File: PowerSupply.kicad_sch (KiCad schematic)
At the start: 45 parts, among them U1 LM399, U2 LT1001

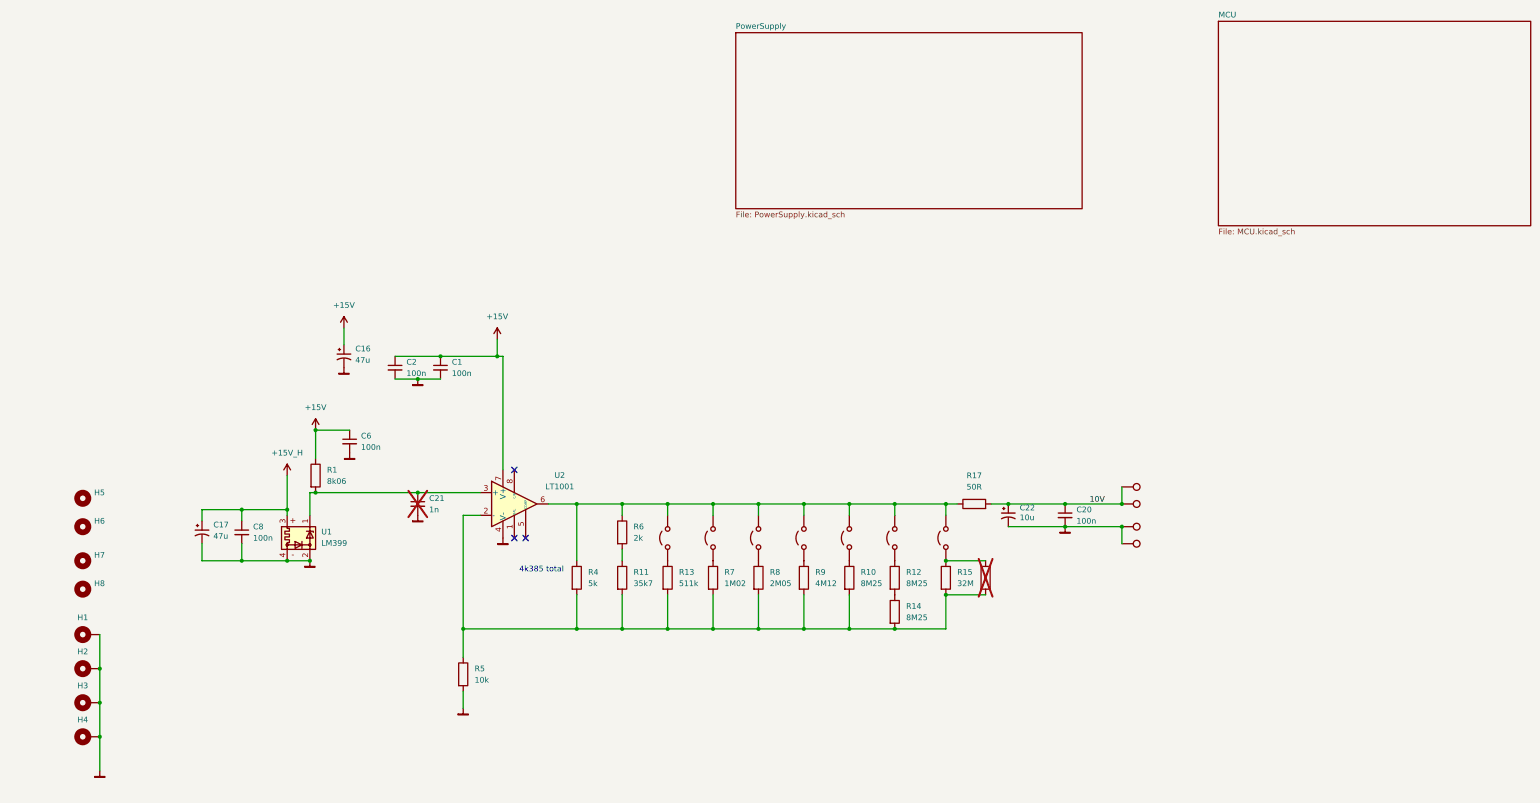
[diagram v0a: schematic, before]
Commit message: Added MCU
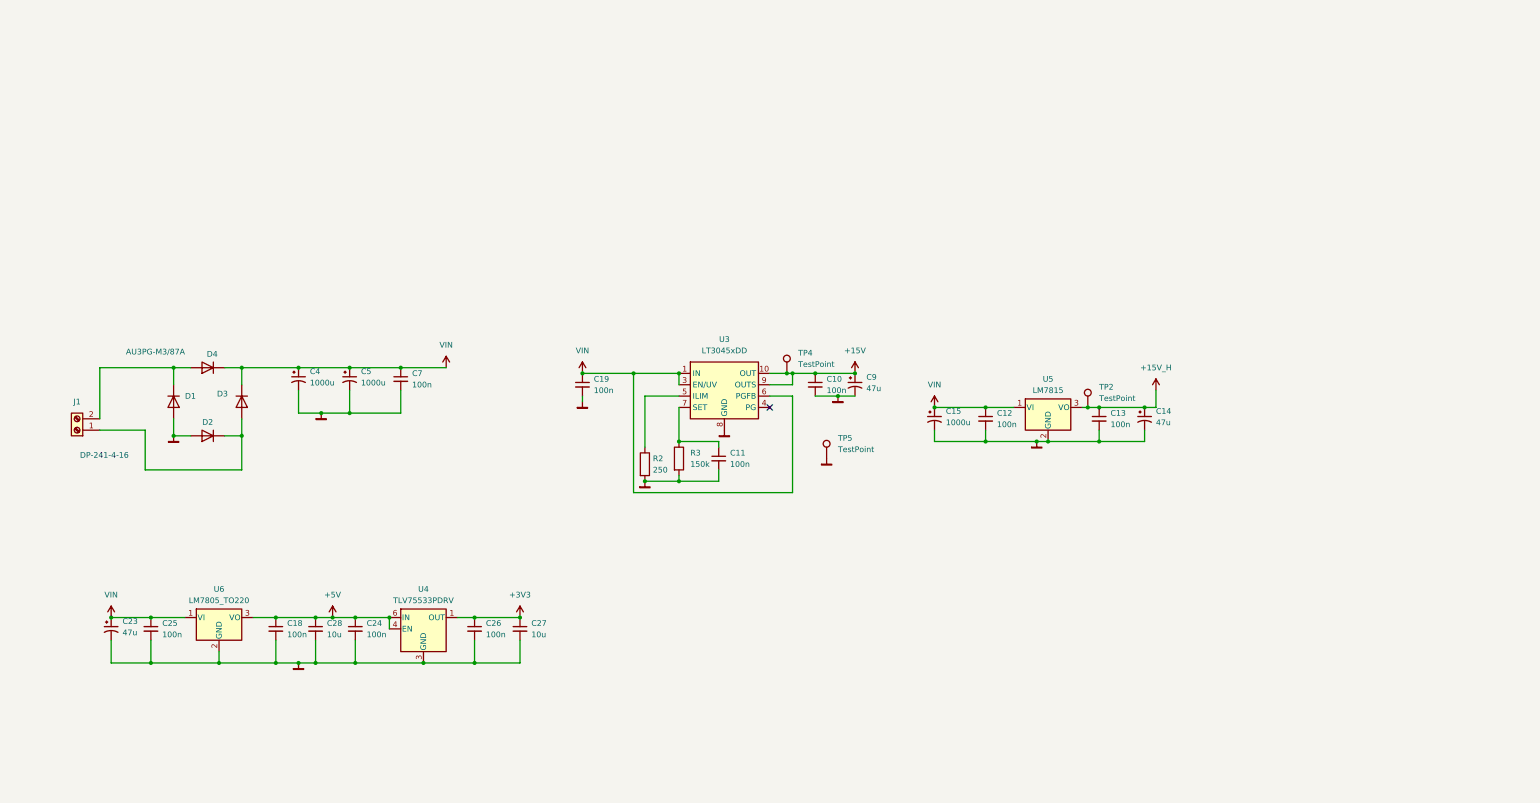
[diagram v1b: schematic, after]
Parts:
- removed C1, C2, C20, C6, C8: 100n, Capacitor_SMD:C_0603_1608Metric, symbol Device:C_Small
- removed C16, C17: 47u, Capacitor_THT:CP_Radial_D5.0mm_P2.00mm, symbol Device:C_Polarized_Small_US
- removed C21: 1n, Capacitor_SMD:C_0603_1608Metric, symbol Device:C_Small
- removed C22: 10u, Capacitor_Tantalum_SMD:CP_EIA-7132-20_AVX-U, symbol Device:C_Polarized_Small_US
- removed H1, H2, H3, H4: MountingHole_Pad, MountingHole:MountingHole_3.2mm_M3_Pad_TopBottom, symbol Mechanical:MountingHole_Pad
- removed H5, H6, H7, H8: MountingHole, MountingHole:MountingHole_3.2mm_M3_DIN965_Pad, symbol Mechanical:MountingHole
- removed JP10, JP11, JP12, JP13, JP14, JP8, JP9: Jumper_2_Open, Jumper:SolderJumper-2_P1.3mm_Open_RoundedPad1.0x1.5mm, symbol Jumper:Jumper_2_Open
- removed R1: 8k06, Resistor_SMD:R_0603_1608Metric, symbol Device:R
- removed R10, R12, R14: 8M25, Resistor_THT:R_Axial_DIN0204_L3.6mm_D1.6mm_P7.62mm_Horizontal, symbol Device:R
- removed R11: 35k7, Resistor_SMD:R_0603_1608Metric, symbol Device:R
- removed R13: 511k, Resistor_SMD:R_0603_1608Metric, symbol Device:R
- removed R15: 32M, Resistor_THT:R_Axial_DIN0207_L6.3mm_D2.5mm_P10.16mm_Horizontal, symbol Device:R
- removed R16: 32M, Resistor_SMD:R_0805_2012Metric, symbol Device:R
- removed R17: 50R, Resistor_SMD:R_0805_2012Metric, symbol Device:R
- removed R4: 5k, LM399VoltageStandard:ZFoilResistor, symbol Device:R
- removed R5: 10k, Resistor_THT:R_Axial_DIN0207_L6.3mm_D2.5mm_P10.16mm_Horizontal, symbol Device:R
- removed R6: 2k, Resistor_SMD:R_1206_3216Metric, symbol Device:R
- removed R7: 1M02, Resistor_SMD:R_0805_2012Metric, symbol Device:R
- removed R8: 2M05, Resistor_SMD:R_0805_2012Metric, symbol Device:R
- removed R9: 4M12, Resistor_THT:R_Axial_DIN0207_L6.3mm_D2.5mm_P10.16mm_Horizontal, symbol Device:R
- removed TP3, TP6, TP7, TP8: TestPoint, TestPoint:TestPoint_Pad_4.0x4.0mm, symbol Connector:TestPoint
- removed U1: LM399, Package_TO_SOT_THT:Analog_TO-46-4_ThermalShield, symbol Reference_Voltage:LM399
- removed U2: LT1001, Package_SO:SOIC-8_3.9x4.9mm_P1.27mm, symbol Amplifier_Operational:LT1012
- added C10, C11, C18, C19, C24, C25, C26, C7: 100n, Capacitor_SMD:C_0603_1608Metric, symbol Device:C_Small
- added C12, C13: 100n, Capacitor_SMD:C_0805_2012Metric, symbol Device:C_Small
- added C14, C23, C9: 47u, Capacitor_THT:CP_Radial_D5.0mm_P2.00mm, symbol Device:C_Polarized_Small_US
- added C15, C4, C5: 1000u, Capacitor_THT:CP_Radial_D10.0mm_P3.80mm, symbol Device:C_Polarized_Small_US
- added C27, C28: 10u, Capacitor_SMD:C_0805_2012Metric, symbol Device:C_Small
- added D1, D2, D3, D4: AU3PG-M3/87A, Package_TO_SOT_SMD:TO-277A, symbol Device:D
- added J1: Screw_Terminal_01x02, TerminalBlock:TerminalBlock_MaiXu_MX126-5.0-02P_1x02_P5.00mm, symbol Connector:Screw_Terminal_01x02
- added R2: 250, Resistor_SMD:R_0603_1608Metric, symbol Device:R
- added R3: 150k, Resistor_SMD:R_0603_1608Metric, symbol Device:R
- added TP2, TP4, TP5: TestPoint, TestPoint:TestPoint_Pad_D1.5mm, symbol Connector:TestPoint
- added U3: LT3045xDD, Package_DFN_QFN:DFN-10-1EP_3x3mm_P0.5mm_EP1.65x2.38mm, symbol Regulator_Linear:LT3045xDD
- added U4: TLV75533PDRV, Package_SON:WSON-6-1EP_2x2mm_P0.65mm_EP1x1.6mm, symbol Regulator_Linear:TLV75533PDRV
- added U5: LM7815, Package_TO_SOT_THT:TO-220-3_Vertical, symbol Regulator_Linear:LM7815_TO220
- added U6: LM7805_TO220, Package_TO_SOT_THT:TO-220-3_Vertical, symbol Regulator_Linear:LM7805_TO220
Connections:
- net +15V: now also C10.1, C9.1, TP4.1, U3.10 (OUT), U3.9 (OUTS)
- net +15V_H: now also C13.1, C14.1, TP2.1, U5.3 (VO)
- net Masa: now also C10.2, C11.2, C12.2, C13.2, C14.2, C15.2, C18.2, C19.2, C23.2, C24.2, C25.2, C26.2, C27.2, C28.2, C4.2, C5.2, C7.2, C9.2, D1.1 (A), D1.2 (A), D2.1 (A), D2.2 (A), R2.2, R3.2, TP5.1, U3.11 (GND), U3.8 (GND), U4.3 (GND), U4.7 (GND), U5.2 (GND), U6.2 (GND)
- new net: R2.1, U3.5 (ILIM)
- new net: C11.1, R3.1, U3.7 (SET)
- new net: D1.3 (K), D4.1 (A), D4.2 (A), J1.2 (Pin_2)
- new net: D2.3 (K), D3.1 (A), D3.2 (A), J1.1 (Pin_1)
- new net +3V3: C26.1, C27.1, U4.1 (OUT)
- new net +5V: C18.1, C24.1, C28.1, U4.4 (EN), U4.6 (IN), U6.3 (VO)
- new net VIN: C12.1, C15.1, C19.1, C23.1, C25.1, C4.1, C5.1, C7.1, D3.3 (K), D4.3 (K), U3.1 (IN), U3.2 (IN), U3.3 (EN/UV), U3.6 (PGFB), U5.1 (VI), U6.1 (VI)
- no-connect marks 3 -> 1
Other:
- removed sheet MCU
- removed sheet PowerSupply
- note added: "DP-241-4-16"
- note removed: "4k385 total"

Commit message: Final Version
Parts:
- added C42, C44, C45: 100n, Capacitor_SMD:C_0603_1608Metric, symbol Device:C_Small
- added R23: 0R1, Resistor_SMD:R_0805_2012Metric, symbol Device:R
- added R24, R27: 4k, Resistor_SMD:R_0603_1608Metric, symbol Device:R
- added R25, R26: 20k, Resistor_SMD:R_0603_1608Metric, symbol Device:R
- added U11: INA180B3, Package_TO_SOT_SMD:SOT-23-5, symbol Amplifier_Current:INA180B3
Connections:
- net +15V: now also R25.1
- net +15V_H: now also R26.1
- net +3V3: now also C42.1, U11.5 (V+)
- net Masa: now also C42.2, C44.2, C45.2, R24.2, R27.2, U11.2 (GND)
- net VIN: now also R23.1, U11.1 (+); no longer C12.1, C15.1, U5.1 (VI)
- new net HEATER_SENSE_L: C12.1, C15.1, R23.2, U11.3 (-), U5.1 (VI)
- new net HEATER_SENSE_OUT: U11.4
- new net HEATER_VOLTAGE_SENSE: C45.1, R26.2, R27.1
- new net REFERENCE_VOLTAGE_SENSE: C44.1, R24.1, R25.2
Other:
- note added: "Current Monitoring"
- note added: "Digital supply"
- note added: "Heater 15V"
- note added: "Rectifier and filtering"
- note added: "Reference 15V"
- note added: "Voltage Monitoring"
- moved on the sheet: C10, C11, C12, C13, C14, C15, C18, C19, C23, C24, C25, C26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

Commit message: Added BOM
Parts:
- C27, C28: Price (none) -> 1,51zł
- D1, D2, D3, D4: Price (none) -> 29.4zł
- R23: Price (none) -> 0,76zł
- U11: Price (none) -> 2,28zł
- U3: Price (none) -> 33,14zł
- U4: Price (none) -> 1,63zł

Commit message: Commit
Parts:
- removed C11: 100n, Capacitor_SMD:C_0603_1608Metric, symbol Device:C_Small
- removed D1, D2, D3, D4: AU3PG-M3/87A, Package_TO_SOT_SMD:TO-277A, symbol Device:D
- removed R2: 250, Resistor_SMD:R_0603_1608Metric, symbol Device:R
- removed R3: 150k, Resistor_SMD:R_0603_1608Metric, symbol Device:R
- removed U3: LT3045xDD, Package_DFN_QFN:DFN-10-1EP_3x3mm_P0.5mm_EP1.65x2.38mm, symbol Regulator_Linear:LT3045xDD
- added C48: 1000u, Capacitor_THT:CP_Radial_D10.0mm_P3.80mm, symbol Device:C_Polarized_Small_US
- added D6: B40C2300-1500A, Diode_THT:Diode_Bridge_19.0x3.5x10.0mm_P5.0mm, symbol Diode_Bridge:B40C2300-1500A
- added U13: LM7815, Package_TO_SOT_THT:TO-220-3_Vertical, symbol Regulator_Linear:LM7815_TO220
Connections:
- net +15V: now also U13.3 (VO)
- net Masa: now also C48.2, D6.1 (-), U13.2 (GND)
- net VIN: now also C48.1, D6.4 (+), U13.1 (VI)
- net at J1.2 (Pin_2): now also D6.2
- net at J1.1 (Pin_1): now also D6.3
- no-connect marks 1 -> 0
